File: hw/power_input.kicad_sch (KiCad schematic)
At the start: 12 parts, among them Q1 100V N-ch, Q2 40V 5mOhm N-ch

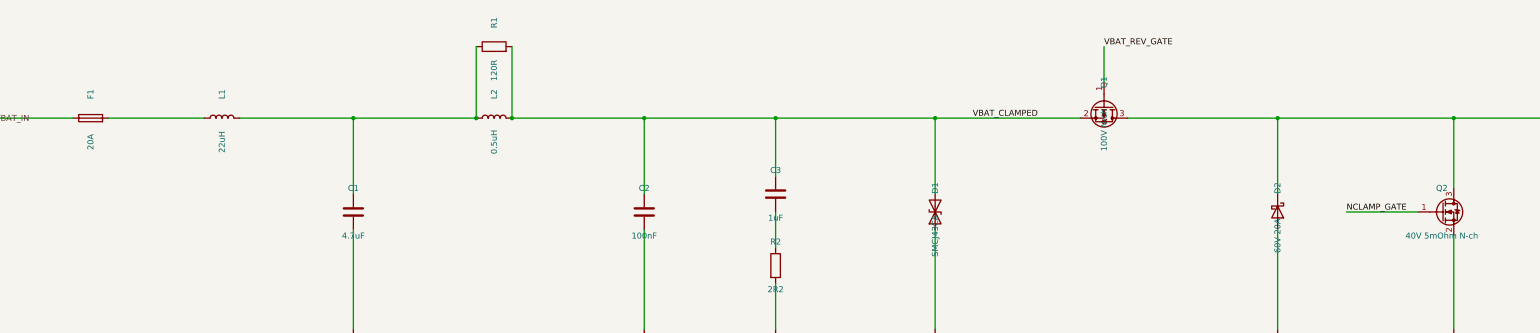
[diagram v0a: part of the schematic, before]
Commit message: Wire the root sheet: the project has a netlist for the first time
Ten sheets each passed their own netlist and the project had none. The
root sheet's ten sheet symbols carried NO hierarchical pins, so a net
name appearing on two sheets was two nets and nothing compared them --
the cross-sheet audit in the last commit was a name comparison, not a
connectivity check.

Each symbol now carries one pin per net its child exports, read OUT of
the child rather than declared in a second list that could drift: 162
pins across the ten, each with a stub and a label. Two labels with the
same name are one net, which is how 162 pins connect without routing
162 wires across a page nobody could read.

Exporting it found the other half of the same problem immediately.
kicad-cli reported annotation errors: every sheet generator allocated
R1, C1, U1 from its own counter, so ten sheets had ten parts called R1.
schlib.REF_BASE gives each sheet its own hundred -- KiCad's own
sheet-number x 100 convention, applied at generation time instead of by
a hand pass in Eeschema. 196 components, no duplicate reference.

hw/check_netlist.py is the gate, and the counterpart to sim/run_sim.py:
that one guards the component values, this one guards the connectivity.
Same rule -- an exemption is not a pass. Every single-pin net is listed
with its reason, and a net that STOPS being single-pin fails the check
until it is removed from the list. An open item that quietly closes is
as much a drift as one that quietly opens.

  196 components, every reference unique
  113 named nets carrying two or more pins
   18 named nets reaching one pin, each a recorded open item
      GND 134 pins, 3V3_MCU 27, VBAT_PROT 12 -- all spanning the project

The root sheet carries those eighteen on the page itself, grouped by
what they wait on, so a reader does not have to run a script to find
which ends are loose.

Full set plots to docs/pdf/ECU-Schematics.pdf, 11 pages.

Two rendering bugs fixed: sheet pin names and their stu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
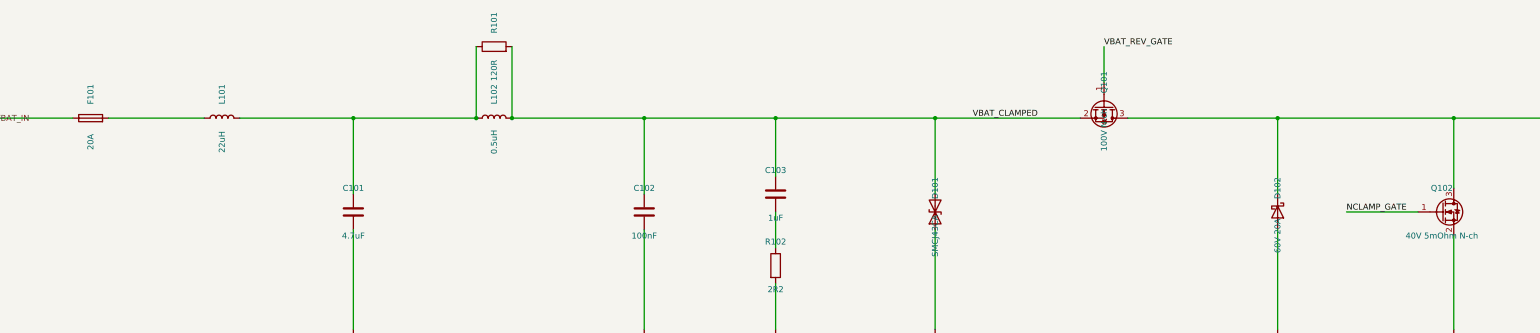
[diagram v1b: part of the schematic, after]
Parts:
- removed C1: 4.7uF, symbol Device:C
- removed C2: 100nF, symbol Device:C
- removed C3: 1uF, symbol Device:C
- removed D1: SMCJ43CA, symbol Device:D_TVS
- removed D2: 60V 20A, symbol Device:D_Schottky
- removed F1: 20A, symbol Device:Fuse
- removed L1: 22uH, symbol Device:L
- removed L2: 0.5uH, symbol Device:L
- removed Q1: 100V N-ch, symbol Device:Q_NMOS_GSD
- removed Q2: 40V 5mOhm N-ch, symbol Device:Q_NMOS_GSD
- removed R1: 120R, symbol Device:R
- removed R2: 2R2, symbol Device:R
- added C101: 4.7uF, symbol Device:C
- added C102: 100nF, symbol Device:C
- added C103: 1uF, symbol Device:C
- added D101: SMCJ43CA, symbol Device:D_TVS
- added D102: 60V 20A, symbol Device:D_Schottky
- added F101: 20A, symbol Device:Fuse
- added L101: 22uH, symbol Device:L
- added L102: 0.5uH, symbol Device:L
- added Q101: 100V N-ch, symbol Device:Q_NMOS_GSD
- added Q102: 40V 5mOhm N-ch, symbol Device:Q_NMOS_GSD
- added R101: 120R, symbol Device:R
- added R102: 2R2, symbol Device:R
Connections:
- net GND: now also C101.2, C102.2, D101.1 (A1), D102.2 (A), Q102.2 (S), R102.2
- net NCLAMP_GATE: now also Q102.1 (G)
- net VBAT_CLAMPED: now also C102.1, C103.1, D101.2 (A2), L102.2, Q101.2 (S), R101.2
- net VBAT_IN: now also F101.1
- net VBAT_PROT: now also D102.1 (K), Q101.3 (D), Q102.3 (D)
- net VBAT_REV_GATE: now also Q101.1 (G)
- new net: C101.1, L101.2, L102.1, R101.1
- new net: C103.2, R102.1
- new net: F101.2, L101.1
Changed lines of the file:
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@@
   (symbol (lib_id "Device:Fuse") (at 52.0 80.0 90) (unit 1)
     (in_bom yes) (on_board yes) (fields_autoplaced)
-    (property "Reference" "F1" (id 0) (at 52 74.92 0)
+    (property "Reference" "F101" (id 0) (at 52 74.92 0)
       (effects (font (size 1.27 1.27)))
     )
@@
   (symbol (lib_id "Device:L") (at 80.0 80.0 90) (unit 1)
     (in_bom yes) (on_board yes) (fields_autoplaced)
-    (property "Reference" "L1" (id 0) (at 80 74.92 0)
+    (property "Reference" "L101" (id 0) (at 80 74.92 0)
       (effects (font (size 1.27 1.27)))
     )
@@
   (symbol (lib_id "Device:C") (at 108.0 100.0 0) (unit 1)
     (in_bom yes) (on_board yes) (fields_autoplaced)
-    (property "Reference" "C1" (id 0) (at 108 94.92 0)
+    (property "Reference" "C101" (id 0) (at 108 94.92 0)
       (effects (font (size 1.27 1.27)))
     )
@@
   (symbol (lib_id "power:GND") (at 108.0 125.0 0) (unit 1)
     (in_bom yes) (on_board yes) (fields_autoplaced)
-    (property "Reference" "#PWR1" (id 0) (at 108 119.92 0)
+    (property "Reference" "#PWR101" (id 0) (at 108 119.92 0)
       (effects (font (size 1.27 1.27)) hide)
     )
@@
   (symbol (lib_id "Device:L") (at 138.0 80.0 90) (unit 1)
     (in_bom yes) (on_board yes) (fields_autoplaced)
-    (property "Reference" "L2" (id 0) (at 138 74.92 0)
+    (property "Reference" "L102" (id 0) (at 138 74.92 0)
       (effects (font (size 1.27 1.27)))
     )
@@
   (symbol (lib_id "Device:R") (at 138.0 64.76 90) (unit 1)
     (in_bom yes) (on_board yes) (fields_autoplaced)
-    (property "Reference" "R1" (id 0) (at 138 59.68000000000001 0)
+    (property "Reference" "R101" (id 0) (at 138 59.68000000000001 0)
       (effects (font (size 1.27 1.27)))
     )
@@
   (symbol (lib_id "Device:C") (at 170.0 100.0 0) (unit 1)
     (in_bom yes) (on_board yes) (fields_autoplaced)
-    (property "Reference" "C2" (id 0) (at 170 94.92 0)
+    (property "Reference" "C102" (id 0) (at 170 94.92 0)
       (effects (font (size 1.27 1.27)))
     )
@@
   (symbol (lib_id "power:GND") (at 170.0 125.0 0) (unit 1)
     (in_bom yes) (on_board yes) (fields_autoplaced)
-    (property "Reference" "#PWR2" (id 0) (at 170 119.92 0)
+    (property "Reference" "#PWR102" (id 0) (at 170 119.92 0)
       (effects (font (size 1.27 1.27)) hide)
     )
@@
   (symbol (lib_id "Device:C") (at 198.0 96.19 0) (unit 1)
     (in_bom yes) (on_board yes) (fields_autoplaced)
-    (property "Reference" "C3" (id 0) (at 198 91.11 0)
+    (property "Reference" "C103" (id 0) (at 198 91.11 0)
       (effects (font (size 1.27 1.27)))
     )
@@
   (symbol (lib_id "Device:R") (at 198.0 111.43 0) (unit 1)
     (in_bom yes) (on_board yes) (fields_autoplaced)
-    (property "Reference" "R2" (id 0) (at 198 106.35000000000001 0)
+    (property "Reference" "R102" (id 0) (at 198 106.35000000000001 0)
       (effects (font (size 1.27 1.27)))
     )
@@
   (symbol (lib_id "power:GND") (at 198.0 125.0 0) (unit 1)
     (in_bom yes) (on_board yes) (fields_autoplaced)
-    (property "Reference" "#PWR3" (id 0) (at 198 119.92 0)
+    (property "Reference" "#PWR103" (id 0) (at 198 119.92 0)
       (effects (font (size 1.27 1.27)) hide)
     )
@@
   (symbol (lib_id "Device:D_TVS") (at 232.0 100.0 90) (unit 1)
     (in_bom yes) (on_board yes) (fields_autoplaced)
-    (property "Reference" "D1" (id 0) (at 232 94.92 0)
+    (property "Reference" "D101" (id 0) (at 232 94.92 0)
       (effects (font (size 1.27 1.27)))
     )
@@
   (symbol (lib_id "power:GND") (at 232.0 125.0 0) (unit 1)
     (in_bom yes) (on_board yes) (fields_autoplaced)
-    (property "Reference" "#PWR4" (id 0) (at 232 119.92 0)
+    (property "Reference" "#PWR104" (id 0) (at 232 119.92 0)
       (effects (font (size 1.27 1.27)) hide)
     )
@@
   (symbol (lib_id "Device:Q_NMOS_GSD") (at 268.0 77.46 270) (unit 1)
     (in_bom yes) (on_board yes) (fields_autoplaced)
-    (property "Reference" "Q1" (id 0) (at 268 72.38 0)
+    (property "Reference" "Q101" (id 0) (at 268 72.38 0)
       (effects (font (size 1.27 1.27)))
     )
@@
   (symbol (lib_id "Device:D_Schottky") (at 305.0 100.0 270) (unit 1)
     (in_bom yes) (on_board yes) (fields_autoplaced)
-    (property "Reference" "D2" (id 0) (at 305 94.92 0)
+    (property "Reference" "D102" (id 0) (at 305 94.92 0)
       (effects (font (size 1.27 1.27)))
     )
@@
   (symbol (lib_id "power:GND") (at 305.0 125.0 0) (unit 1)
     (in_bom yes) (on_board yes) (fields_autoplaced)
-    (property "Reference" "#PWR5" (id 0) (at 305 119.92 0)
+    (property "Reference" "#PWR105" (id 0) (at 305 119.92 0)
       (effects (font (size 1.27 1.27)) hide)
     )
@@
   (symbol (lib_id "Device:Q_NMOS_GSD") (at 340.0 100.0 0) (unit 1)
     (in_bom yes) (on_board yes) (fields_autoplaced)
-    (property "Reference" "Q2" (id 0) (at 340 94.92 0)
+    (property "Reference" "Q102" (id 0) (at 340 94.92 0)
       (effects (font (size 1.27 1.27)))
     )
@@
   (symbol (lib_id "power:GND") (at 342.54 125.0 0) (unit 1)
     (in_bom yes) (on_board yes) (fields_autoplaced)
-    (property "Reference" "#PWR6" (id 0) (at 342.54 119.92 0)
-      (effects (font (size 1.27 1.27)) hide)
-    )
+    (property "Reference" "#PWR106" (id 0) (at 342.54 119.92 0)
+      (effects (font (size 1.27 1.27)) hide)
+    )
